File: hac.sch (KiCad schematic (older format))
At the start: 18 parts, among them J1 AudioJack3_Ground, U1 STM32F405RGTx, U2 TLV320AIC23BPW

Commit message: schm done
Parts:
- added C12, C13, C14, C15, C18, C19, C22, C23, C24, C25, C27, C9: 100n, Capacitor_SMD:C_0603_1608Metric_Pad1.05x0.95mm_HandSolder, symbol Device:C_Small
- added C16, C17, C5, C6: 20p, Capacitor_SMD:C_0603_1608Metric_Pad1.05x0.95mm_HandSolder, symbol Device:C_Small
- added C20, C21: 330n, Capacitor_SMD:C_0603_1608Metric_Pad1.05x0.95mm_HandSolder, symbol Device:C_Small
- added C26: 10u, symbol Device:CP1_Small
- added C7, C8: 2.2u, Capacitor_SMD:C_0603_1608Metric_Pad1.05x0.95mm_HandSolder, symbol Device:C_Small
- added D1: 0, symbol Device:LED_Small
- added D2: 1, symbol Device:LED_Small
- added D3: 2, symbol Device:LED_Small
- added D4: 3, symbol Device:LED_Small
- added D5: 4, symbol Device:LED_Small
- added D6: 5, symbol Device:LED_Small
- added D7: 6, symbol Device:LED_Small
- added D8: 7, symbol Device:LED_Small
- added J3: USB_B_Micro, symbol Connector:USB_B_Micro
- added L1: FB, symbol Device:L_Core_Ferrite_Small
- added L3, L4: 1m, symbol Device:L
- added R10, R11, R12, R13, R14, R15, R8, R9: 1k, Resistor_SMD:R_0603_1608Metric_Pad1.05x0.95mm_HandSolder, symbol Device:R_Small
- added R18, R19, R22, R23, R25, R26, R5: 0, Resistor_SMD:R_0603_1608Metric_Pad1.05x0.95mm_HandSolder, symbol Device:R_Small
- added R20, R21: DNP, Resistor_SMD:R_0603_1608Metric_Pad1.05x0.95mm_HandSolder, symbol Device:R_Small
- added R24: 100k, Resistor_SMD:R_0603_1608Metric_Pad1.05x0.95mm_HandSolder, symbol Device:R_Small
- added R6: 220, Resistor_SMD:R_0603_1608Metric_Pad1.05x0.95mm_HandSolder, symbol Device:R_Small
- added R7: 10k, Resistor_SMD:R_0603_1608Metric_Pad1.05x0.95mm_HandSolder, symbol Device:R_Small
- added TP1: C3, symbol Connector:TestPoint
- added TP10: I2S2WS, symbol Connector:TestPoint
- added TP11: I2C2SD, symbol Connector:TestPoint
- added TP12: SPICS, symbol Connector:TestPoint
- added TP13: USBDM, symbol Connector:TestPoint
- added TP14: I2S2CK, symbol Connector:TestPoint
- added TP15: SPISCK, symbol Connector:TestPoint
- added TP16: I2C2SDEXT, symbol Connector:TestPoint
- added TP17: USBDP, symbol Connector:TestPoint
- added TP18: SPIMISO, symbol Connector:TestPoint
- added TP19: SPIMOSI, symbol Connector:TestPoint
- added TP2: C2, symbol Connector:TestPoint
- added TP20: I2S3SD, symbol Connector:TestPoint
- added TP21: VUSB, symbol Connector:TestPoint
- added TP22: LOUT, symbol Connector:TestPoint
- added TP23: LIN, symbol Connector:TestPoint
- added TP24: ROUT, symbol Connector:TestPoint
- added TP25: RIN, symbol Connector:TestPoint
- added TP26: 3.3V, symbol Connector:TestPoint
- added TP27: 3.3VA, symbol Connector:TestPoint
- added TP3: C1, symbol Connector:TestPoint
- added TP4: I2SMCK, symbol Connector:TestPoint
- added TP5: BOOT0, symbol Connector:TestPoint
- added TP6: C0, symbol Connector:TestPoint
- added TP7: NRST, symbol Connector:TestPoint
- added TP8: I2S3WS, symbol Connector:TestPoint
- added TP9: I2S3CK, symbol Connector:TestPoint
- added U3, U4: L78L33_SOT89, Package_TO_SOT_SMD:SOT-89-3, symbol Regulator_Linear:L78L33_SOT89
- added Y1, Y2: 8MHz, symbol Device:Crystal_Small
- gave numbers to parts that had none: 7
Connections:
- net GNDA is gone; now on net GND: C1.2, C2.2, J1.S, J2.S, R16.1, R17.1, R3.1, R4.1, U2.15 (AGND)
- net +3.3VA: now also C25.1, TP27.1, U4.1 (OUT)
- net +3V3: now also U2.22 (MODE), C24.1, L1.1, TP26.1, U3.1 (OUT)
- net GND: now also J1.G, J2.G, U1.12 (VSSA), U1.18 (VSS), U1.63 (VSS), U2.11 (HPGND), C12.2, C13.2, C14.2, C15.2, C16.2, C17.2, C18.2, C19.2, C20.2, C21.2, C22.2, C23.2, C24.2, C25.2, C26.2, C27.2, C5.2, C6.2, C7.2, C8.2, C9.2, D1.1 (K), D2.1 (K), D3.1 (K), D4.1 (K), D5.1 (K), D6.1 (K), D7.1 (K), D8.1 (K), J3.5 (GND), J3.6 (Shield), R24.1, R7.1, U3.2 (GND), U4.2 (GND)
- net LLINEIN: now also TP23.1
- net LLINEOUT: now also TP22.1; no longer U2.13 (ROUT)
- net RLINEIN: now also TP25.1
- net RLINEOUT: now also U2.13 (ROUT), TP24.1
- net at U1.1 (VBAT): now also U1.13 (VDDA), U1.19 (VDD), U1.32 (VDD), U1.48 (VDD), U1.64 (VDD), C12.1, C13.1, C14.1, C15.1, C27.1, C9.1, L1.2
- net at U1.10 (PC2): now also TP2.1
- net at U1.11 (PC3): now also TP1.1
- net at U1.2 (PC13): now also R13.2
- net SPI_CS: now reaches U1.20 (PA4)
- net SPI_CS: now also U2.21 (~CS~), TP12.1
- net SPI_SCK: now reaches U1.21 (PA5)
- net SPI_SCK: now also U2.24 (SCLK), TP15.1
- net SPI1_MISO: now reaches U1.22 (PA6)
- net SPI1_MISO: now also TP18.1
- net SPI_MOSI: now reaches U1.23 (PA7)
- net SPI_MOSI: now also U2.23 (SDIN), TP19.1
- net at U1.3 (PC14): now also R14.2
- net at U1.31 (VCAP_1): now also C7.1
- net I2S_WSI: now reaches U1.33 (PB12)
- net I2S_WSI: now also U2.7 (LRCOUT), TP10.1
- net I2S_CK: now reaches U1.34 (PB13)
- net I2S_CK: now also U2.3 (BCLK), R18.2, TP14.1
- net I2S2ext_SD: now reaches U1.35 (PB14)
- net I2S2ext_SD: now also R20.2, TP16.1
- net I2S_SDI: now reaches U1.36 (PB15)
- net I2S_SDI: now also U2.6 (DOUT), TP11.1
- net I2S_MCK: now reaches U1.37 (PC6)
- net I2S_MCK: now also R21.2, TP4.1
- net at U1.39 (PC8): now also R8.2
- net at U1.4 (PC15): now also R15.2
- net at U1.40 (PC9): now also R9.2
- net USB_DM: now reaches U1.44 (PA11)
- net USB_DM: now also R26.2, TP13.1
- net USB_DP: now reaches U1.45 (PA12)
- net USB_DP: now also R25.2, TP17.1
- net at U1.47 (VCAP_2): now also C8.1
- net at U1.5 (PH0): now also R5.1
- net I2S_WSO: now reaches U1.50 (PA15)
- net I2S_WSO: now also U2.5 (LRCIN), TP8.1
- net at U1.51 (PC10): now also R10.2
- net at U1.52 (PC11): now also R11.2
- net at U1.53 (PC12): now also R12.2
- net I2S3_CK: now reaches U1.55 (PB3)
- net I2S3_CK: now also R18.1, TP9.1
- net I2S3_SD: now reaches U1.57 (PB5)
- net I2S3_SD: now also R19.2, TP20.1
- net at U1.6 (PH1): now also R6.2
- net at U1.60 (BOOT0): now also R7.2, TP5.1
- net at U1.7 (NRST): now also TP7.1
- net at U1.8 (PC0): now also TP6.1
- net at U1.9 (PC1): now also TP3.1
- net at L2.2, U2.1 (BVDD), U2.27 (DVDD): now also C18.1, C19.1
- net at L5.2, U2.14 (AVDD): now also C22.1
- net at U2.16 (VMID): now also C23.1, C26.1
- net at U2.25 (XTI/MCK): now also R21.1, R22.1
- net at U2.26 (XTO): now also R23.2
- net I2S_SDO: now reaches U2.4 (DIN)
- net I2S_SDO: now also R19.1, R20.1
- new net: J3.1 (VBUS), L3.1, L4.1, TP21.1
- new net: J3.2 (D-), R26.1
- new net: J3.3 (D+), R25.1
- new net: J3.4 (ID), R24.2
- new net: C20.1, L3.2, U3.3 (IN)
- new net: C21.1, L4.2, U4.3 (IN)
- new net: C5.1, R5.2, Y1.1
- new net: C6.1, R6.1, Y1.2
- new net: C16.1, R22.2, Y2.1
- new net: C17.1, R23.1, Y2.2
- new net: D1.2 (A), R8.1
- new net: D2.2 (A), R9.1
- new net: D3.2 (A), R10.1
- new net: D4.2 (A), R11.1
- new net: D5.2 (A), R12.1
- new net: D6.2 (A), R13.1
- new net: D7.2 (A), R14.1
- new net: D8.2 (A), R15.1
- no-connect marks 2 -> 29
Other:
- moved on the sheet: L2, L5, U1, U2

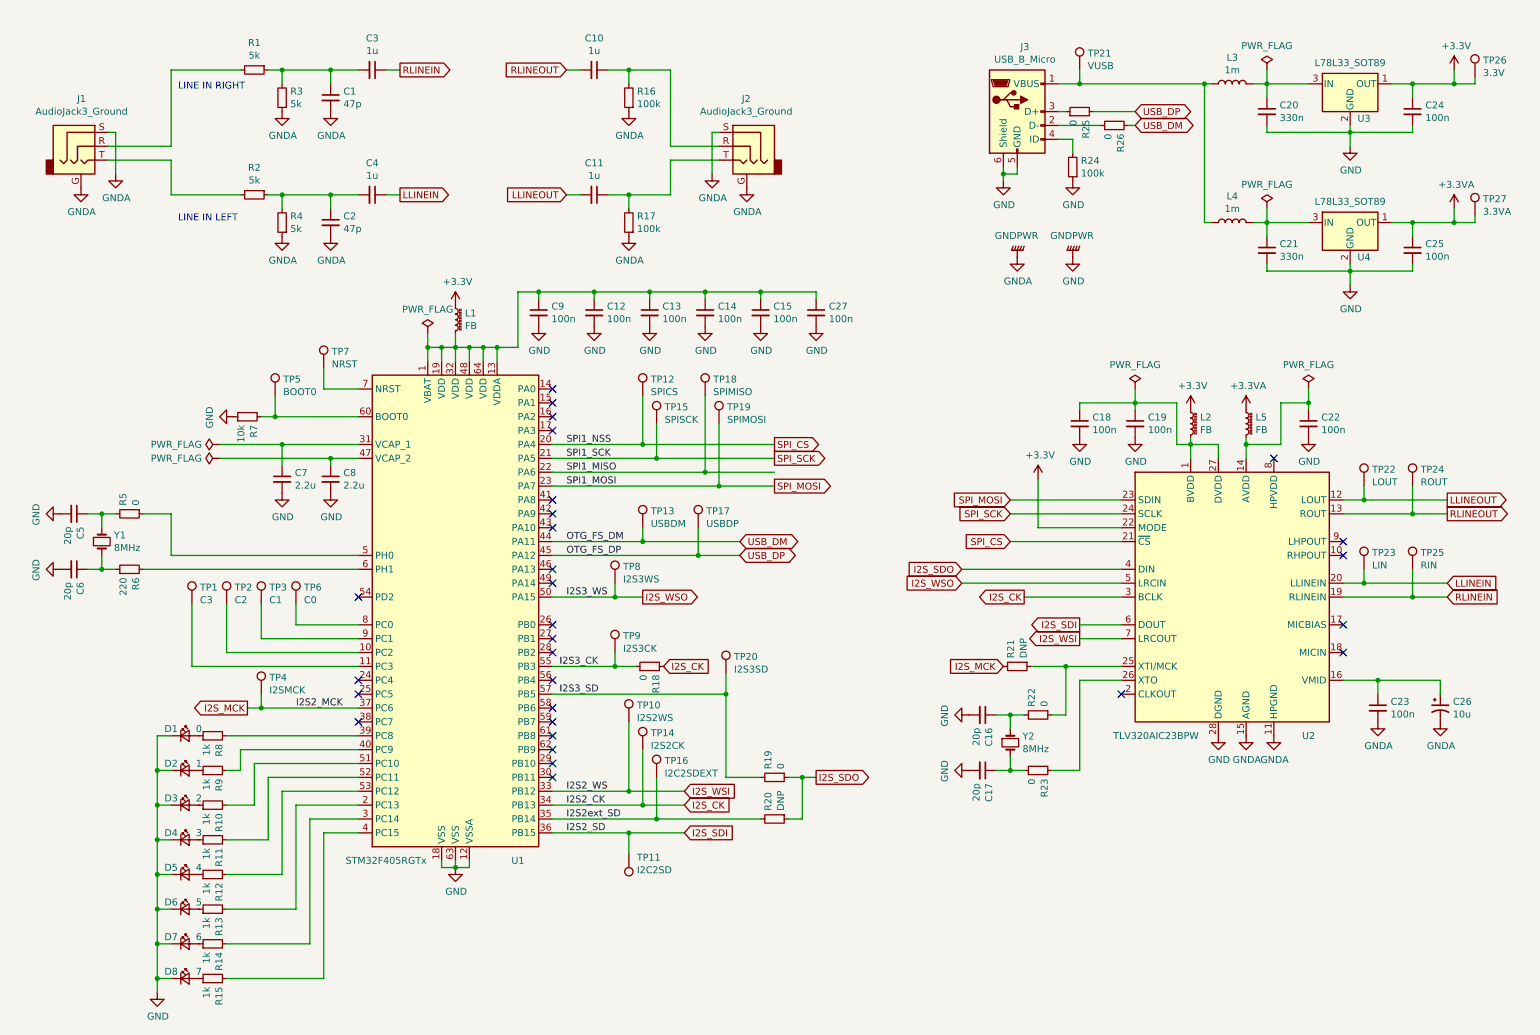
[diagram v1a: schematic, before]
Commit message: schm fixes + footprints done
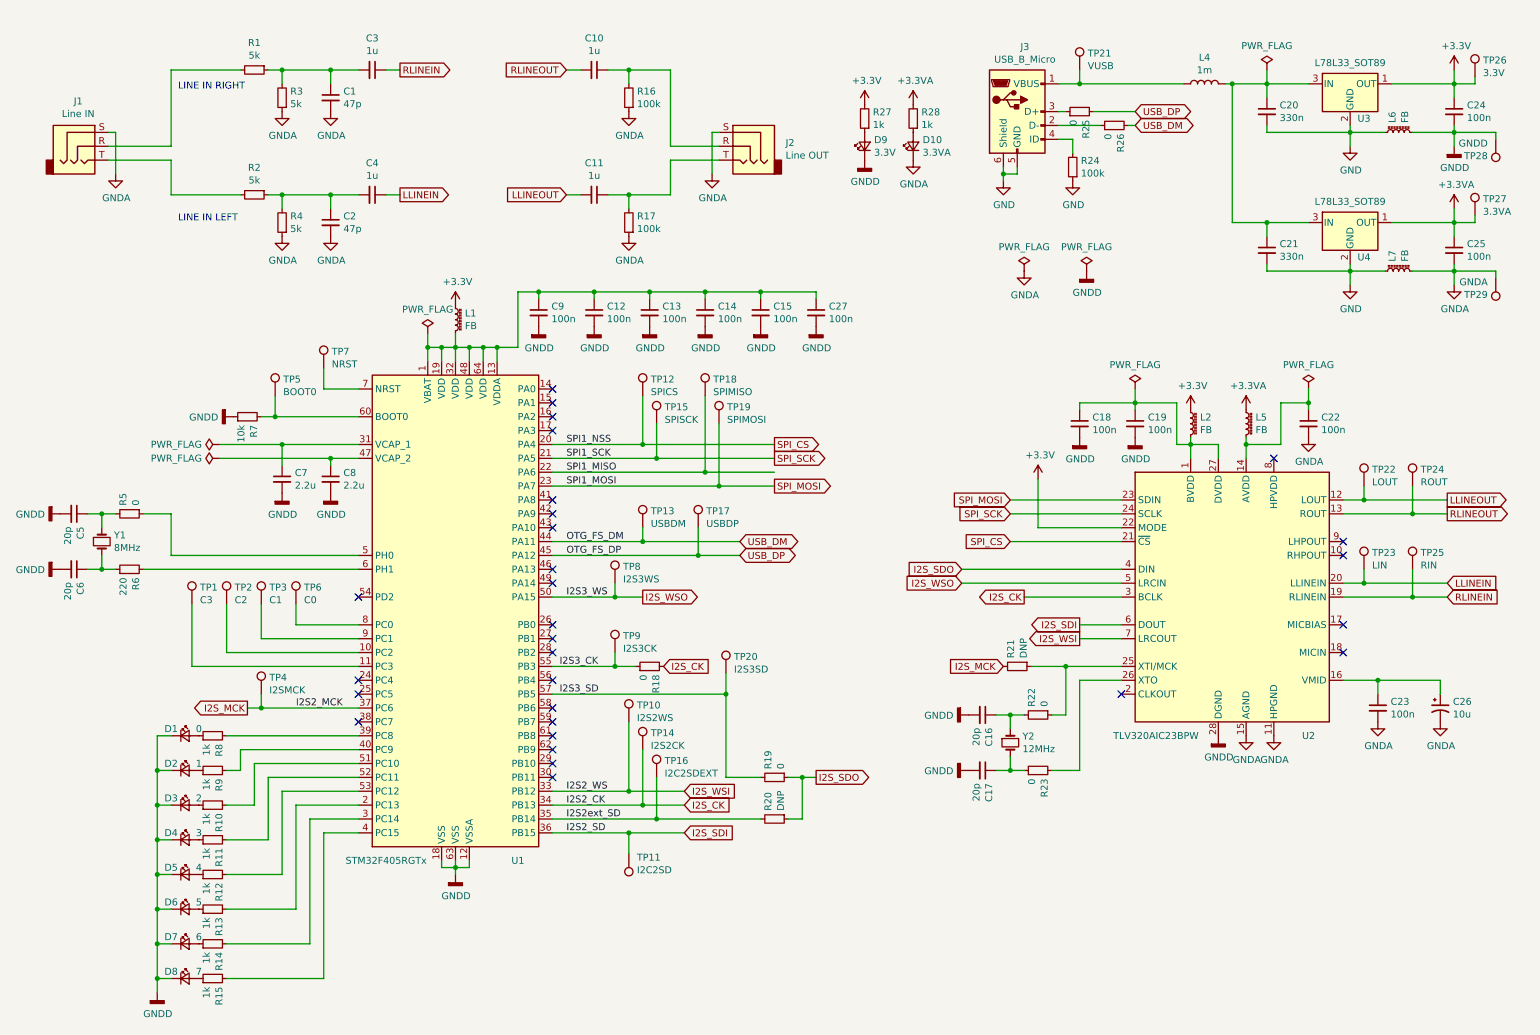
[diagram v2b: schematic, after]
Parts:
- removed J1, J2: AudioJack3_Ground, Connector_Audio:Jack_3.5mm_CUI_SJ1-3533NG_Horizontal, symbol Connector:AudioJack3_Ground
- removed L3: 1m, symbol Device:L
- added D10: 3.3VA, LED_SMD:LED_0603_1608Metric, symbol Device:LED_Small
- added D9: 3.3V, LED_SMD:LED_0603_1608Metric, symbol Device:LED_Small
- added J1: Line IN, Connector_Audio:Jack_3.5mm_CUI_SJ1-3533NG_Horizontal, symbol Connector:AudioJack3
- added J2: Line OUT, Connector_Audio:Jack_3.5mm_CUI_SJ1-3533NG_Horizontal, symbol Connector:AudioJack3
- added L6, L7: FB, Inductor_SMD:L_0805_2012Metric, symbol Device:L_Core_Ferrite_Small
- added R27, R28: 1k, Resistor_SMD:R_0603_1608Metric, symbol Device:R_Small
- added TP28: GNDD, TestPoint:TestPoint_Pad_D1.5mm, symbol Connector:TestPoint
- added TP29: GNDA, TestPoint:TestPoint_Pad_D1.5mm, symbol Connector:TestPoint
- C1, C12, C13, C14, C15, C16, C17, C18, C19, C2, C20, C21, C22, C23, C24, C25, C27, C5, C6, C9: footprint Capacitor_SMD:C_0603_1608Metric_Pad1.05x0.95mm_HandSolder -> Capacitor_SMD:C_0603_1608Metric
- C10, C11, C3, C4, C7, C8: footprint Capacitor_SMD:C_0603_1608Metric_Pad1.05x0.95mm_HandSolder -> Capacitor_SMD:C_0805_2012Metric
- C26: footprint (none) -> Capacitor_Tantalum_SMD:CP_EIA-3216-18_Kemet-A
- D1, D2, D3, D4, D5, D6, D7, D8: footprint (none) -> LED_SMD:LED_0603_1608Metric
- J3: footprint (none) -> Connector_USB:USB_Micro-B_Molex-105017-0001
- L1, L2, L5: footprint (none) -> Inductor_SMD:L_0805_2012Metric
- L4: footprint (none) -> Inductor_SMD:L_7.3x7.3_H4.5; RS (none) -> 617-1530; Wurth (none) -> 74477730
- R1, R10, R11, R12, R13, R14, R15, R16, R17, R18, R19, R2, R20, R21, R22, R23, R24, R25, R26, R3, R4, R5, R6, R7, R8, R9: footprint Resistor_SMD:R_0603_1608Metric_Pad1.05x0.95mm_HandSolder -> Resistor_SMD:R_0603_1608Metric
- TP1, TP10, TP11, TP12, TP13, TP14, TP15, TP16, TP17, TP18, TP19, TP2, TP20, TP21, TP22, TP23, TP24, TP25, TP26, TP27, TP3, TP4, TP5, TP6, TP7, TP8, TP9: footprint (none) -> TestPoint:TestPoint_Pad_D1.5mm
- Y1: footprint (none) -> Crystal:Crystal_SMD_HC49-SD
- Y2: value 8MHz -> 12MHz; footprint (none) -> Crystal:Crystal_SMD_HC49-SD
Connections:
- net +3.3VA: now also R28.2
- net +3V3: now also R27.2
- net GND: now also L6.1, L7.1; no longer C1.2, C12.2, C13.2, C14.2, C15.2, C16.2, C17.2, C18.2, C19.2, C2.2, C22.2, C23.2, C24.2, C25.2, C26.2, C27.2, C5.2, C6.2, C7.2, C8.2, C9.2, D1.1 (K), D2.1 (K), D3.1 (K), D4.1 (K), D5.1 (K), D6.1 (K), D7.1 (K), D8.1 (K), R16.1, R17.1, R3.1, R4.1, R7.1, U1.12 (VSSA), U1.18 (VSS), U1.63 (VSS), U2.11 (HPGND), U2.15 (AGND), U2.28 (DGND)
- net at R1.2: now also J1.R
- net at R2.2: now also J1.T
- net at C10.1, R16.2: now also J2.R
- net at C11.1, R17.2: now also J2.T
- net at C20.1, U3.3 (IN): now also C21.1, L4.2, U4.3 (IN)
- new net: D9.2 (A), R27.1
- new net: D10.2 (A), R28.1
- new net GNDA: C1.2, C2.2, C22.2, C23.2, C25.2, C26.2, D10.1 (K), J1.S, J2.S, L7.2, R16.1, R17.1, R3.1, R4.1, TP29.1, U2.11 (HPGND), U2.15 (AGND)
- new net GNDD: C12.2, C13.2, C14.2, C15.2, C16.2, C17.2, C18.2, C19.2, C24.2, C27.2, C5.2, C6.2, C7.2, C8.2, C9.2, D1.1 (K), D2.1 (K), D3.1 (K), D4.1 (K), D5.1 (K), D6.1 (K), D7.1 (K), D8.1 (K), D9.1 (K), L6.2, R7.1, TP28.1, U1.12 (VSSA), U1.18 (VSS), U1.63 (VSS), U2.28 (DGND)
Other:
- moved on the sheet: C24, C25, L4

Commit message: component placement done
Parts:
- removed J1: Line IN, Connector_Audio:Jack_3.5mm_CUI_SJ1-3533NG_Horizontal, symbol Connector:AudioJack3
- removed J2: Line OUT, Connector_Audio:Jack_3.5mm_CUI_SJ1-3533NG_Horizontal, symbol Connector:AudioJack3
- added C28, C29: 100u, Capacitor_Tantalum_SMD:CP_EIA-6032-28_Kemet-C, symbol Device:CP1_Small
- added C30: 100n, Capacitor_SMD:C_0603_1608Metric, symbol Device:C_Small
- added H1, H2, H3, H4: MountingHole, MountingHole:MountingHole_3.2mm_M3, symbol Mechanical:MountingHole
- added J1: LIN, Connector_Audio:Jack_3.5mm_Neutrik_NMJ6HCD2_Horizontal, symbol Connector:AudioJack3_Switch
- added J2: LOUT, Connector_Audio:Jack_3.5mm_Neutrik_NMJ6HCD2_Horizontal, symbol Connector:AudioJack3_Switch
- added J4: HPOUT, Connector_Audio:Jack_3.5mm_Neutrik_NMJ6HCD2_Horizontal, symbol Connector:AudioJack3_Switch
- added R29, R30: 100k, Resistor_SMD:R_0603_1608Metric, symbol Device:R_Small
- added R31: 3.3, Resistor_SMD:R_0603_1608Metric, symbol Device:R_Small
- added TP30: LHP, TestPoint:TestPoint_Pad_D1.5mm, symbol Connector:TestPoint
- added TP31: RHP, TestPoint:TestPoint_Pad_D1.5mm, symbol Connector:TestPoint
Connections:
- net +3V3: no longer U2.22 (MODE)
- net GNDA: now also C30.2, J1.S, J2.S, J4.S, R29.1, R30.1
- net 3V3_STM: now reaches C12.1, C13.1, C14.1, C15.1, C27.1, C9.1, L1.2, U1.1 (VBAT), U1.13 (VDDA), U1.19 (VDD), U1.32 (VDD), U1.48 (VDD), U1.64 (VDD)
- net LED7: now reaches U1.17 (PA3)
- net LED7: now also R15.2
- net at U1.2 (PC13): no longer R13.2
- net LED6: now reaches U1.24 (PC4)
- net LED6: now also R14.2
- net LED5: now reaches U1.25 (PC5)
- net LED5: now also R13.2
- net LED4: now reaches U1.26 (PB0)
- net LED4: now also R12.2
- net LED3: now reaches U1.27 (PB1)
- net LED3: now also R11.2
- net LED2: now reaches U1.28 (PB2)
- net LED2: now also R10.2
- net LED1: now reaches U1.29 (PB10)
- net LED1: now also R9.2
- net at U1.3 (PC14): no longer R14.2
- net LED0: now reaches U1.30 (PB11)
- net LED0: now also R8.2
- net at U1.39 (PC8): no longer R8.2
- net at U1.4 (PC15): no longer R15.2
- net at U1.40 (PC9): no longer R9.2
- net at U1.51 (PC10): no longer R10.2
- net at U1.52 (PC11): no longer R11.2
- net at U1.53 (PC12): no longer R12.2
- net at C18.1, C19.1, L2.2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: now also U2.22 (MODE)
- net RHPOUT: now reaches U2.10 (RHPOUT)
- net RHPOUT: now also C28.1, TP31.1
- net at C22.1, U2.14 (AVDD): now also R31.1; no longer L5.2
- net at U2.8 (HPVDD): now also L5.2, C30.1, R31.2
- net LHPOUT: now reaches U2.9 (LHPOUT)
- net LHPOUT: now also C29.1, TP30.1
- net at R2.2: now also J1.T
- net at R1.2: now also J1.R
- net at C10.1, R16.2: now also J2.R
- net at C11.1, R17.2: now also J2.T
- new net: C28.2, J4.R, R29.2
- new net: C29.2, J4.T, R30.2
- no-connect marks 29 -> 27
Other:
- note removed: "LINE IN LEFT"
- note removed: "LINE IN RIGHT\n"
- moved on the sheet: C1, C10, C11, C2, C20, C21, C24, C25, C3, C4, D1, D10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

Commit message: some routing done
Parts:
- added TP32: CLKOUT, TestPoint:TestPoint_Pad_D1.5mm, symbol Connector:TestPoint
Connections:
- net at U2.2 (CLKOUT): now also TP32.1
- net USB_DM renamed USB_D-
- net USB_DP renamed USB_D+
- no-connect marks 27 -> 34
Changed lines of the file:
@@
 $EndComp
 Text GLabel 8450 1100 2    50   BiDi ~ 0
-USB_DM
+USB_D-
 Text GLabel 8450 1000 2    50   BiDi ~ 0
-USB_DP
+USB_D+
 Wire Wire Line
 	8450 1000 8150 1000
@@
 OTG_FS_DP
 Text GLabel 5650 4400 2    50   BiDi ~ 0
-USB_DP
+USB_D+
 Text GLabel 5650 4300 2    50   BiDi ~ 0
-USB_DM
+USB_D-
 $Comp
 L Regulator_Linear:L78L33_SOT89 U3
@@
 Connection ~ 5800 2500
 NoConn ~ 2900 5600
-NoConn ~ 8400 5400
 $Comp
 L power:PWR_FLAG #FLG0101
@@
 Text GLabel 4300 3500 2    50   Output ~ 0
 LED7
+$Comp
+L Connector:TestPoint TP32
+U 1 1 5C479A42
+P 8250 6100
+F 0 "TP32" H 8308 6220 50  0000 L CNN
+F 1 "CLKOUT" H 8308 6129 50  0000 L CNN
+F 2 "TestPoint:TestPoint_Pad_D1.5mm" H 8450 6100 50  0001 C CNN
+F 3 "~" H 8450 6100 50  0001 C CNN
+	1    8250 6100
+	-1   0    0    1
+$EndComp
+Wire Wire Line
+	8400 5400 8250 5400
+Wire Wire Line
+	8250 5400 8250 6100
+NoConn ~ 2900 6400
+NoConn ~ 2900 6300
+NoConn ~ 2900 6200
+NoConn ~ 2900 6100
+NoConn ~ 2900 6000
+NoConn ~ 2900 5900
+NoConn ~ 2900 5800
+NoConn ~ 2900 5700
+$Comp
+L power:PWR_FLAG #FLG0103
+U 1 1 5C5619AE
+P 10100 2800
+F 0 "#FLG0103" H 10100 2875 50  0001 C CNN
+F 1 "PWR_FLAG" H 10100 2974 50  0000 C CNN
+F 2 "" H 10100 2800 50  0001 C CNN
+F 3 "~" H 10100 2800 50  0001 C CNN
+	1    10100 2800
+	1    0    0    -1
+$EndComp
+Wire Wire Line
+	10100 2800 10100 2900
+Connection ~ 10100 2900
+$Comp
+L power:PWR_FLAG #FLG0109
+U 1 1 5C57919F
+P 9750 3200
+F 0 "#FLG0109" H 9750 3275 50  0001 C CNN
+F 1 "PWR_FLAG" H 9750 3374 50  0000 C CNN
+F 2 "" H 9750 3200 50  0001 C CNN
+F 3 "~" H 9750 3200 50  0001 C CNN
+	1    9750 3200
+	1    0    0    -1
+$EndComp
+Wire Wire Line
+	9750 3200 9750 3300
+Connection ~ 9750 3300
 $EndSCHEMATC

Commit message: routing almost done
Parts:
- added TP33, TP34: GND, TestPoint:TestPoint_Pad_D1.5mm, symbol Connector:TestPoint
- added TP35, TP37, TP39, TP41: GNDD, TestPoint:TestPoint_Pad_D1.5mm, symbol Connector:TestPoint
- added TP36, TP38, TP40: GNDA, TestPoint:TestPoint_Pad_D1.5mm, symbol Connector:TestPoint
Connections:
- net GND: now also TP33.1, TP34.1
- net GNDA: now also TP36.1, TP38.1, TP40.1
- net GNDD: now also TP35.1, TP37.1, TP39.1, TP41.1
